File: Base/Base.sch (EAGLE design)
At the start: 20 parts

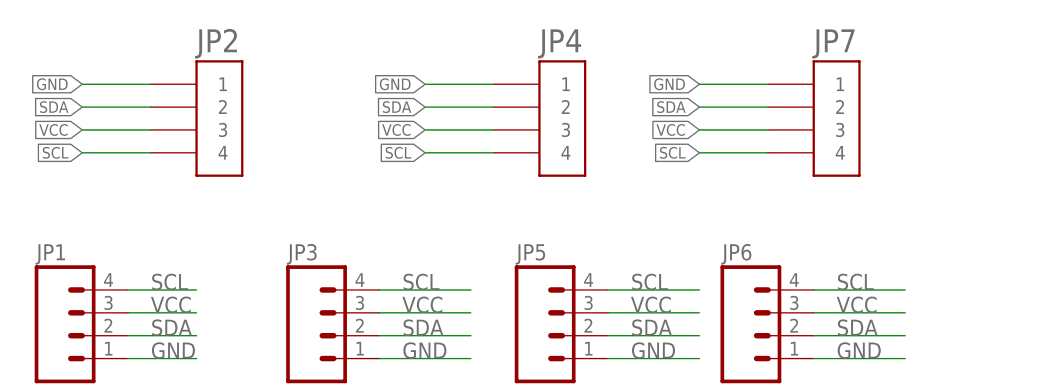
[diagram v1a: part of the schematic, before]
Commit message: Updated to grove compatible connector footprints
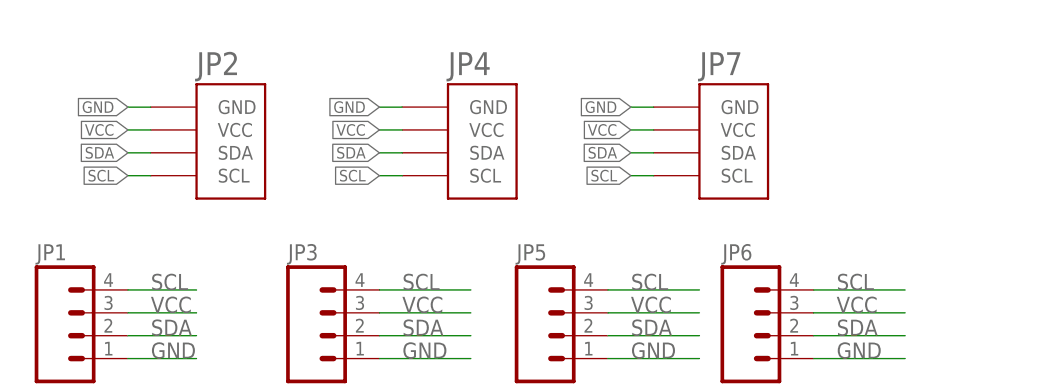
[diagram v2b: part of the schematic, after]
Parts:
- JP2, JP4, JP7: value HEADER-1X4-JST-PA-SIDE-SMD -> HEADER-MODULO; device Modulo:HEADER-1X4-JST-PA-SIDE-SMD -> Modulo:HEADER-MODULO
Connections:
- net GND: now also JP2.GND, JP4.GND, JP7.GND; no longer JP2.1, JP4.1, JP7.1
- net SCL: now also JP2.SCL, JP4.SCL, JP7.SCL; no longer JP2.4, JP4.4, JP7.4
- net SDA: now also JP2.SDA, JP4.SDA, JP7.SDA; no longer JP2.2, JP4.2, JP7.2
- net VCC: now also JP2.VCC, JP4.VCC, JP7.VCC; no longer JP2.3, JP4.3, JP7.3
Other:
- moved on the sheet: JP2, JP4, JP7
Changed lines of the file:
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@@
 <attribute name="NOBOM" value="1"/>
 </part>
-<part name="JP4" library="Modulo" deviceset="HEADER-1X4" device="-JST-PA-SIDE-SMD" value="HEADER-1X4-JST-PA-SIDE-SMD"/>
-<part name="JP7" library="Modulo" deviceset="HEADER-1X4" device="-JST-PA-SIDE-SMD" value="HEADER-1X4-JST-PA-SIDE-SMD"/>
-<part name="JP2" library="Modulo" deviceset="HEADER-1X4" device="-JST-PA-SIDE-SMD" value="HEADER-1X4-JST-PA-SIDE-SMD"/>
 <part name="H3" library="Modulo" deviceset="HOLE" device="#2" value="HOLE#2">
 <attribute name="NOBOM" value="1"/>
@@
 <part name="H8" library="Modulo" deviceset="HOLE" device="#2"/>
 <part name="H6" library="Modulo" deviceset="HOLE" device="#2"/>
+<part name="JP2" library="Modulo" deviceset="HEADER-MODULO" device=""/>
+<part name="JP4" library="Modulo" deviceset="HEADER-MODULO" device=""/>
+<part name="JP7" library="Modulo" deviceset="HEADER-MODULO" device=""/>
 </parts>
 <sheets>
@@
 <attribute name="NOBOM" x="152.4" y="81.28" size="1.016" layer="96" display="off"/>
 </instance>
-<instance part="JP4" gate="G$1" x="124.46" y="147.32"/>
-<instance part="JP7" gate="G$1" x="154.94" y="147.32"/>
-<instance part="JP2" gate="G$1" x="86.36" y="147.32"/>
 <instance part="H3" gate="G$1" x="162.56" y="81.28">
 <attribute name="NOBOM" x="162.56" y="81.28" size="1.016" layer="96" display="off"/>
@@
 <instance part="H8" gate="G$1" x="182.88" y="73.66"/>
 <instance part="H6" gate="G$1" x="172.72" y="73.66"/>
+<instance part="JP2" gate="G$1" x="88.9" y="142.24"/>
+<instance part="JP4" gate="G$1" x="116.84" y="142.24"/>
+<instance part="JP7" gate="G$1" x="144.78" y="142.24"/>
 </instances>
 <busses>
@@
 </segment>
 <segment>
-<wire x1="149.86" y1="144.78" x2="142.24" y2="144.78" width="0.1524" layer="91"/>
-<label x="142.24" y="144.78" size="1.27" layer="95" rot="R180" xref="yes"/>
-<pinref part="JP7" gate="G$1" pin="3"/>
-</segment>
-<segment>
-<wire x1="81.28" y1="144.78" x2="73.66" y2="144.78" width="0.1524" layer="91"/>
-<label x="73.66" y="144.78" size="1.27" layer="95" rot="R180" xref="yes"/>
-<pinref part="JP2" gate="G$1" pin="3"/>
-</segment>
-<segment>
-<wire x1="119.38" y1="144.78" x2="111.76" y2="144.78" width="0.1524" layer="91"/>
-<label x="111.76" y="144.78" size="1.27" layer="95" rot="R180" xref="yes"/>
-<pinref part="JP4" gate="G$1" pin="3"/>
+<pinref part="JP2" gate="G$1" pin="VCC"/>
+<wire x1="81.28" y1="144.78" x2="78.74" y2="144.78" width="0.1524" layer="91"/>
+<label x="78.74" y="144.78" size="1.27" layer="95" rot="R180" xref="yes"/>
+</segment>
+<segment>
+<pinref part="JP4" gate="G$1" pin="VCC"/>
+<wire x1="109.22" y1="144.78" x2="106.68" y2="144.78" width="0.1524" layer="91"/>
+<label x="106.68" y="144.78" size="1.27" layer="95" rot="R180" xref="yes"/>
+</segment>
+<segment>
+<pinref part="JP7" gate="G$1" pin="VCC"/>
+<wire x1="137.16" y1="144.78" x2="134.62" y2="144.78" width="0.1524" layer="91"/>
+<label x="134.62" y="144.78" size="1.27" layer="95" rot="R180" xref="yes"/>
 </segment>
 </net>
@@
 </segment>
 <segment>
-<wire x1="149.86" y1="149.86" x2="142.24" y2="149.86" width="0.1524" layer="91"/>
-<label x="142.24" y="149.86" size="1.27" layer="95" rot="R180" xref="yes"/>
-<pinref part="JP7" gate="G$1" pin="1"/>
-</segment>
-<segment>
-<wire x1="81.28" y1="149.86" x2="73.66" y2="149.86" width="0.1524" layer="91"/>
-<label x="73.66" y="149.86" size="1.27" layer="95" rot="R180" xref="yes"/>
-<pinref part="JP2" gate="G$1" pin="1"/>
-</segment>
-<segment>
-<wire x1="119.38" y1="149.86" x2="111.76" y2="149.86" width="0.1524" layer="91"/>
-<label x="111.76" y="149.86" size="1.27" layer="95" rot="R180" xref="yes"/>
-<pinref part="JP4" gate="G$1" pin="1"/>
+<pinref part="JP2" gate="G$1" pin="GND"/>
+<wire x1="81.28" y1="147.32" x2="78.74" y2="147.32" width="0.1524" layer="91"/>
+<label x="78.74" y="147.32" size="1.27" layer="95" rot="R180" xref="yes"/>
+</segment>
+<segment>
+<pinref part="JP4" gate="G$1" pin="GND"/>
+<wire x1="109.22" y1="147.32" x2="106.68" y2="147.32" width="0.1524" layer="91"/>
+<label x="106.68" y="147.32" size="1.27" layer="95" rot="R180" xref="yes"/>
+</segment>
+<segment>
+<pinref part="JP7" gate="G$1" pin="GND"/>
+<wire x1="137.16" y1="147.32" x2="134.62" y2="147.32" width="0.1524" layer="91"/>
+<label x="134.62" y="147.32" size="1.27" layer="95" rot="R180" xref="yes"/>
 </segment>
 </net>
@@
 </segment>
 <segment>
-<wire x1="149.86" y1="147.32" x2="142.24" y2="147.32" width="0.1524" layer="91"/>
-<label x="142.24" y="147.32" size="1.27" layer="95" rot="R180" xref="yes"/>
-<pinref part="JP7" gate="G$1" pin="2"/>
-</segment>
-<segment>
-<wire x1="81.28" y1="147.32" x2="73.66" y2="147.32" width="0.1524" layer="91"/>
-<label x="73.66" y="147.32" size="1.27" layer="95" rot="R180" xref="yes"/>
-<pinref part="JP2" gate="G$1" pin="2"/>
-</segment>
-<segment>
-<wire x1="119.38" y1="147.32" x2="111.76" y2="147.32" width="0.1524" layer="91"/>
-<label x="111.76" y="147.32" size="1.27" layer="95" rot="R180" xref="yes"/>
-<pinref part="JP4" gate="G$1" pin="2"/>
+<pinref part="JP2" gate="G$1" pin="SDA"/>
+<wire x1="81.28" y1="142.24" x2="78.74" y2="142.24" width="0.1524" layer="91"/>
+<label x="78.74" y="142.24" size="1.27" layer="95" rot="R180" xref="yes"/>
+</segment>
+<segment>
+<pinref part="JP4" gate="G$1" pin="SDA"/>
+<wire x1="109.22" y1="142.24" x2="106.68" y2="142.24" width="0.1524" layer="91"/>
+<label x="106.68" y="142.24" size="1.27" layer="95" rot="R180" xref="yes"/>
+</segment>
+<segment>
+<pinref part="JP7" gate="G$1" pin="SDA"/>
+<wire x1="137.16" y1="142.24" x2="134.62" y2="142.24" width="0.1524" layer="91"/>
+<label x="134.62" y="142.24" size="1.27" layer="95" rot="R180" xref="yes"/>
 </segment>
 </net>
@@
 </segment>
 <segment>
-<wire x1="149.86" y1="142.24" x2="142.24" y2="142.24" width="0.1524" layer="91"/>
-<label x="142.24" y="142.24" size="1.27" layer="95" rot="R180" xref="yes"/>
-<pinref part="JP7" gate="G$1" pin="4"/>
-</segment>
-<segment>
-<wire x1="81.28" y1="142.24" x2="73.66" y2="142.24" width="0.1524" layer="91"/>
-<label x="73.66" y="142.24" size="1.27" layer="95" rot="R180" xref="yes"/>
-<pinref part="JP2" gate="G$1" pin="4"/>
-</segment>
-<segment>
-<wire x1="119.38" y1="142.24" x2="111.76" y2="142.24" width="0.1524" layer="91"/>
-<label x="111.76" y="142.24" size="1.27" layer="95" rot="R180" xref="yes"/>
-<pinref part="JP4" gate="G$1" pin="4"/>
-</segment>
-</net>
+<pinref part="JP2" gate="G$1" pin="SCL"/>
+<wire x1="81.28" y1="139.7" x2="78.74" y2="139.7" width="0.1524" layer="91"/>
+<label x="78.74" y="139.7" size="1.27" layer="95" rot="R180" xref="yes"/>
+</segment>
+<segment>
+<pinref part="JP4" gate="G$1" pin="SCL"/>
+<wire x1="109.22" y1="139.7" x2="106.68" y2="139.7" width="0.1524" layer="91"/>
+<label x="106.68" y="139.7" size="1.27" layer="95" rot="R180" xref="yes"/>
+</segment>
+<segment>
+<pinref part="JP7" gate="G$1" pin="SCL"/>
+<wire x1="137.16" y1="139.7" x2="134.62" y2="139.7" width="0.1524" layer="91"/>
+<label x="134.62" y="139.7" size="1.27" layer="95" rot="R180" xref="yes"/>
+</segment>
+</net>

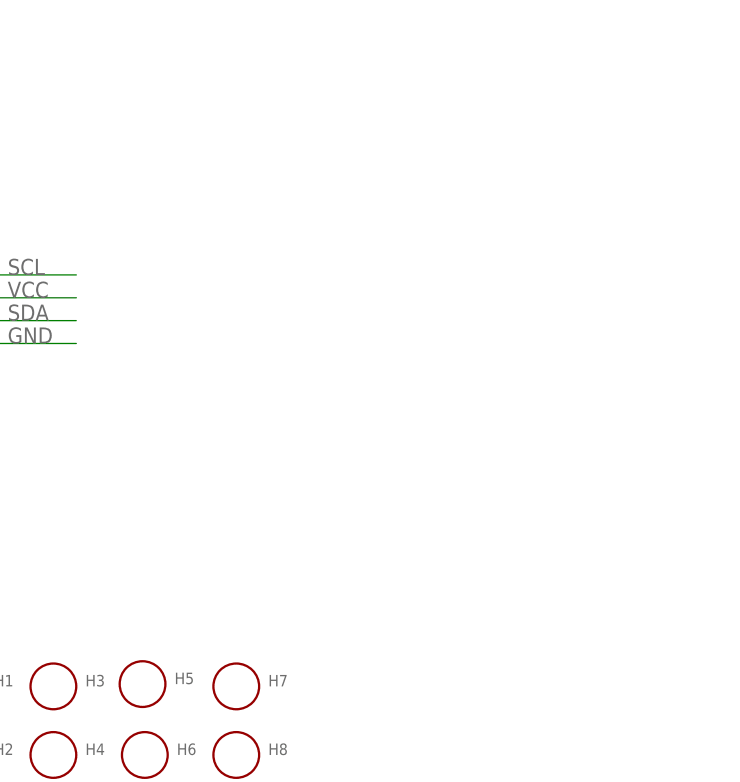
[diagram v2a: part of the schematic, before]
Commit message: Tented vias Updated extension cable connectors Added 3.3v regulator and clamping diodes
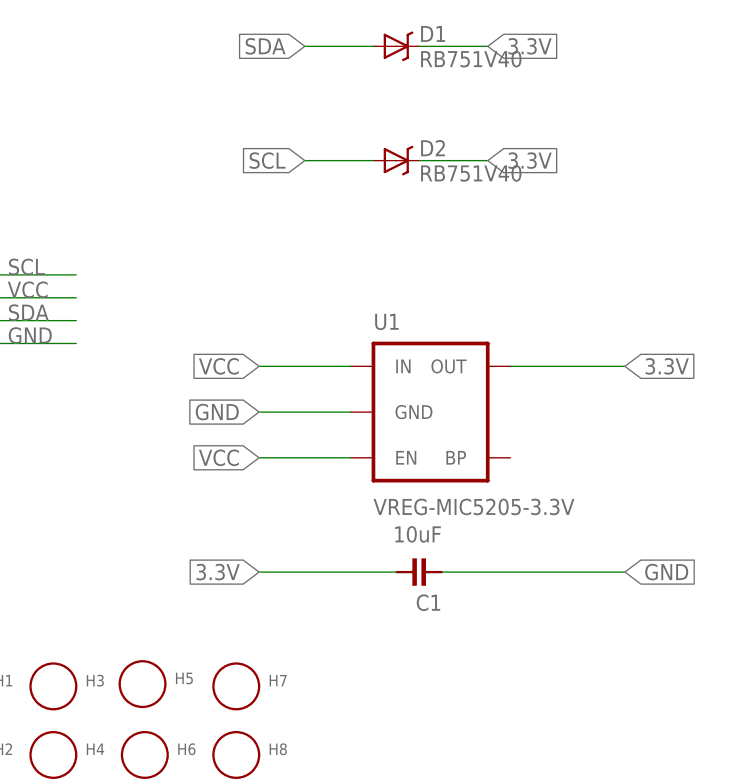
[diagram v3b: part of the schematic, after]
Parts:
- added C1: 10uF, Modulo:CAPACITOR-10UF
- added D1, D2: RB751V40, Modulo:DIODE-SCHOTTKY-BAT60A
- added U1: VREG-MIC5205-3.3V, Modulo:VREG-MIC5205-3.3V
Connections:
- new net 3.3V: C1.1, D1.C, D2.C, U1.OUT
- net GND: now also C1.2, U1.GND
- net SCL: now also D2.A
- net SDA: now also D1.A
- net VCC: now also U1.EN, U1.IN
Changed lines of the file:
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@@
 <part name="JP4" library="Modulo" deviceset="HEADER-MODULO" device=""/>
 <part name="JP7" library="Modulo" deviceset="HEADER-MODULO" device=""/>
+<part name="D1" library="Modulo" deviceset="DIODE-SCHOTTKY" device="-BAT60A" value="RB751V40">
+<attribute name="PARTNUM" value="RB751V40"/>
+</part>
+<part name="D2" library="Modulo" deviceset="DIODE-SCHOTTKY" device="-BAT60A" value="RB751V40">
+<attribute name="PARTNUM" value="RB751V40"/>
+</part>
+<part name="U1" library="Modulo" deviceset="VREG-MIC5205" device="-3.3V"/>
+<part name="C1" library="Modulo" deviceset="CAPACITOR" device="-10UF" value="10uF"/>
 </parts>
 <sheets>
@@
 <instance part="JP4" gate="G$1" x="116.84" y="142.24"/>
 <instance part="JP7" gate="G$1" x="144.78" y="142.24"/>
+<instance part="D1" gate="G$1" x="200.66" y="152.4"/>
+<instance part="D2" gate="G$1" x="200.66" y="139.7"/>
+<instance part="U1" gate="G$1" x="205.74" y="111.76"/>
+<instance part="C1" gate="G$1" x="203.2" y="93.98" rot="R90"/>
 </instances>
 <busses>
@@
 <label x="134.62" y="144.78" size="1.27" layer="95" rot="R180" xref="yes"/>
 </segment>
+<segment>
+<pinref part="U1" gate="G$1" pin="IN"/>
+<wire x1="195.58" y1="116.84" x2="185.42" y2="116.84" width="0.1524" layer="91"/>
+<label x="185.42" y="116.84" size="1.778" layer="95" rot="R180" xref="yes"/>
+</segment>
+<segment>
+<pinref part="U1" gate="G$1" pin="EN"/>
+<wire x1="195.58" y1="106.68" x2="185.42" y2="106.68" width="0.1524" layer="91"/>
+<label x="185.42" y="106.68" size="1.778" layer="95" rot="R180" xref="yes"/>
+</segment>
 </net>
 <net name="GND" class="0">
@@
 <label x="134.62" y="147.32" size="1.27" layer="95" rot="R180" xref="yes"/>
 </segment>
+<segment>
+<pinref part="U1" gate="G$1" pin="GND"/>
+<wire x1="195.58" y1="111.76" x2="185.42" y2="111.76" width="0.1524" layer="91"/>
+<label x="185.42" y="111.76" size="1.778" layer="95" rot="R180" xref="yes"/>
+</segment>
+<segment>
+<pinref part="C1" gate="G$1" pin="2"/>
+<wire x1="205.74" y1="93.98" x2="226.06" y2="93.98" width="0.1524" layer="91"/>
+<label x="226.06" y="93.98" size="1.778" layer="95" xref="yes"/>
+</segment>
 </net>
 <net name="SDA" class="0">
@@
 <label x="134.62" y="142.24" size="1.27" layer="95" rot="R180" xref="yes"/>
 </segment>
+<segment>
+<pinref part="D1" gate="G$1" pin="A"/>
+<wire x1="198.12" y1="152.4" x2="190.5" y2="152.4" width="0.1524" layer="91"/>
+<label x="190.5" y="152.4" size="1.778" layer="95" rot="R180" xref="yes"/>
+</segment>
 </net>
 <net name="SCL" class="0">
@@
 <label x="134.62" y="139.7" size="1.27" layer="95" rot="R180" xref="yes"/>
 </segment>
-</net>
+<segment>
+<pinref part="D2" gate="G$1" pin="A"/>
+<wire x1="198.12" y1="139.7" x2="190.5" y2="139.7" width="0.1524" layer="91"/>
+<label x="190.5" y="139.7" size="1.778" layer="95" rot="R180" xref="yes"/>
+</segment>
+</net>
+<net name="3.3V" class="0">
+<segment>
+<pinref part="C1" gate="G$1" pin="1"/>
+<wire x1="200.66" y1="93.98" x2="185.42" y2="93.98" width="0.1524" layer="91"/>
+<label x="185.42" y="93.98" size="1.778" layer="95" rot="R180" xref="yes"/>
+</segment>
+<segment>
+<pinref part="U1" gate="G$1" pin="OUT"/>
+<wire x1="213.36" y1="116.84" x2="226.06" y2="116.84" width="0.1524" layer="91"/>
+<label x="226.06" y="116.84" size="1.778" layer="95" xref="yes"/>
+</segment>
+<segment>
+<pinref part="D1" gate="G$1" pin="C"/>
+<wire x1="203.2" y1="152.4" x2="210.82" y2="152.4" width="0.1524" layer="91"/>
+<label x="210.82" y="152.4" size="1.778" layer="95" xref="yes"/>
+</segment>
+<segment>
+<pinref part="D2" gate="G$1" pin="C"/>
+<wire x1="203.2" y1="139.7" x2="210.82" y2="139.7" width="0.1524" layer="91"/>
+<label x="210.82" y="139.7" size="1.778" layer="95" xref="yes"/>
+</segment>
+</net>

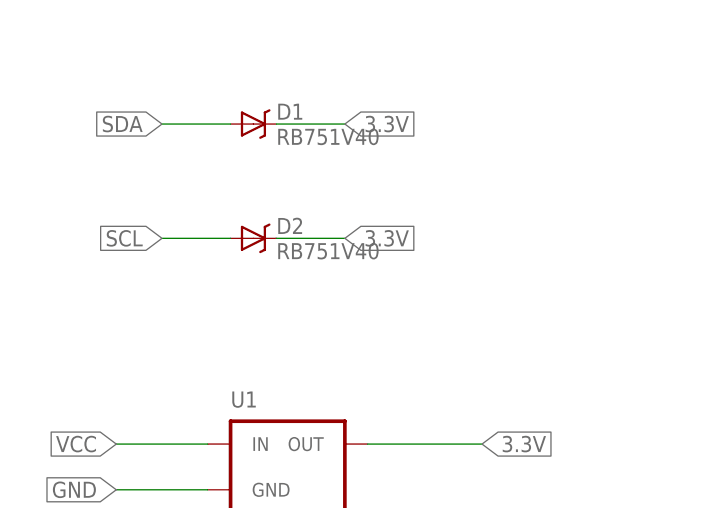
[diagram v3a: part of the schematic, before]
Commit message: Various small tweaks based on testing and feedback from manufacturer.
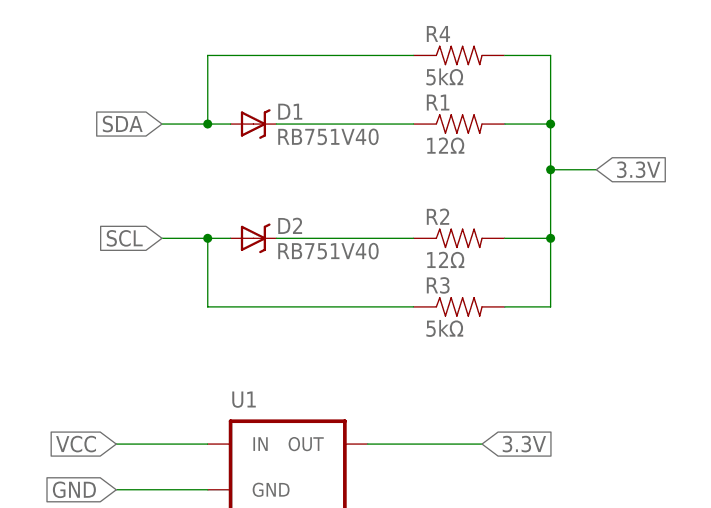
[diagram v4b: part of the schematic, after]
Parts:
- added R1, R2: 12Ω, Modulo:RESISTOR-12Ω
- added R3, R4: 5kΩ, Modulo:RESISTOR-5KΩ
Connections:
- new net N$1: D2.C, R2.1
- new net N$3: D1.C, R1.1
- net 3.3V: now also R1.2, R2.2, R3.2, R4.2; no longer D1.C, D2.C
- net SCL: now also R3.1
- net SDA: now also R4.1
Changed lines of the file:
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@@
 <part name="U1" library="Modulo" deviceset="VREG-MIC5205" device="-3.3V"/>
 <part name="C1" library="Modulo" deviceset="CAPACITOR" device="-10UF" value="10uF"/>
+<part name="R1" library="Modulo" deviceset="RESISTOR" device="-12Ω" value="12Ω"/>
+<part name="R2" library="Modulo" deviceset="RESISTOR" device="-12Ω" value="12Ω"/>
+<part name="R3" library="Modulo" deviceset="RESISTOR" device="-5KΩ" value="5kΩ"/>
+<part name="R4" library="Modulo" deviceset="RESISTOR" device="-5KΩ" value="5kΩ"/>
 </parts>
 <sheets>
@@
 <instance part="U1" gate="G$1" x="205.74" y="111.76"/>
 <instance part="C1" gate="G$1" x="203.2" y="93.98" rot="R90"/>
+<instance part="R1" gate="G$1" x="223.52" y="152.4"/>
+<instance part="R2" gate="G$1" x="223.52" y="139.7"/>
+<instance part="R3" gate="G$1" x="223.52" y="132.08"/>
+<instance part="R4" gate="G$1" x="223.52" y="160.02"/>
 </instances>
 <busses>
@@
 <segment>
 <pinref part="D1" gate="G$1" pin="A"/>
-<wire x1="198.12" y1="152.4" x2="190.5" y2="152.4" width="0.1524" layer="91"/>
+<wire x1="198.12" y1="152.4" x2="195.58" y2="152.4" width="0.1524" layer="91"/>
 <label x="190.5" y="152.4" size="1.778" layer="95" rot="R180" xref="yes"/>
+<pinref part="R4" gate="G$1" pin="1"/>
+<wire x1="195.58" y1="152.4" x2="190.5" y2="152.4" width="0.1524" layer="91"/>
+<wire x1="218.44" y1="160.02" x2="195.58" y2="160.02" width="0.1524" layer="91"/>
+<wire x1="195.58" y1="160.02" x2="195.58" y2="152.4" width="0.1524" layer="91"/>
+<junction x="195.58" y="152.4"/>
 </segment>
 </net>
@@
 <segment>
 <pinref part="D2" gate="G$1" pin="A"/>
-<wire x1="198.12" y1="139.7" x2="190.5" y2="139.7" width="0.1524" layer="91"/>
+<wire x1="198.12" y1="139.7" x2="195.58" y2="139.7" width="0.1524" layer="91"/>
 <label x="190.5" y="139.7" size="1.778" layer="95" rot="R180" xref="yes"/>
+<pinref part="R3" gate="G$1" pin="1"/>
+<wire x1="195.58" y1="139.7" x2="190.5" y2="139.7" width="0.1524" layer="91"/>
+<wire x1="218.44" y1="132.08" x2="195.58" y2="132.08" width="0.1524" layer="91"/>
+<wire x1="195.58" y1="132.08" x2="195.58" y2="139.7" width="0.1524" layer="91"/>
+<junction x="195.58" y="139.7"/>
 </segment>
 </net>
@@
 </segment>
 <segment>
+<pinref part="R3" gate="G$1" pin="2"/>
+<wire x1="228.6" y1="132.08" x2="233.68" y2="132.08" width="0.1524" layer="91"/>
+<wire x1="233.68" y1="132.08" x2="233.68" y2="139.7" width="0.1524" layer="91"/>
+<pinref part="R4" gate="G$1" pin="2"/>
+<wire x1="233.68" y1="139.7" x2="233.68" y2="147.32" width="0.1524" layer="91"/>
+<wire x1="233.68" y1="147.32" x2="233.68" y2="152.4" width="0.1524" layer="91"/>
+<wire x1="233.68" y1="152.4" x2="233.68" y2="160.02" width="0.1524" layer="91"/>
+<wire x1="233.68" y1="160.02" x2="228.6" y2="160.02" width="0.1524" layer="91"/>
+<pinref part="R1" gate="G$1" pin="2"/>
+<wire x1="228.6" y1="152.4" x2="233.68" y2="152.4" width="0.1524" layer="91"/>
+<pinref part="R2" gate="G$1" pin="2"/>
+<wire x1="228.6" y1="139.7" x2="233.68" y2="139.7" width="0.1524" layer="91"/>
+<wire x1="233.68" y1="147.32" x2="238.76" y2="147.32" width="0.1524" layer="91"/>
+<label x="238.76" y="147.32" size="1.778" layer="95" xref="yes"/>
+<junction x="233.68" y="152.4"/>
+<junction x="233.68" y="147.32"/>
+<junction x="233.68" y="139.7"/>
+</segment>
+</net>
+<net name="N$1" class="0">
+<segment>
+<pinref part="D2" gate="G$1" pin="C"/>
+<pinref part="R2" gate="G$1" pin="1"/>
+<wire x1="203.2" y1="139.7" x2="218.44" y2="139.7" width="0.1524" layer="91"/>
+</segment>
+</net>
+<net name="N$3" class="0">
+<segment>
+<pinref part="R1" gate="G$1" pin="1"/>
 <pinref part="D1" gate="G$1" pin="C"/>
-<wire x1="203.2" y1="152.4" x2="210.82" y2="152.4" width="0.1524" layer="91"/>
-<label x="210.82" y="152.4" size="1.778" layer="95" xref="yes"/>
-</segment>
-<segment>
-<pinref part="D2" gate="G$1" pin="C"/>
-<wire x1="203.2" y1="139.7" x2="210.82" y2="139.7" width="0.1524" layer="91"/>
-<label x="210.82" y="139.7" size="1.778" layer="95" xref="yes"/>
-</segment>
-</net>
+<wire x1="218.44" y1="152.4" x2="203.2" y2="152.4" width="0.1524" layer="91"/>
+</segment>
+</net>

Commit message: Added unique board prefixes to part numbers due to CM requirements
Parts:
- added 2-FOOT1, 2-FOOT2, 2-FOOT3, 2-FOOT4: FOOT, Modulo:FOOT
- renumbered C1 to 2-C1, D1 to 2-D1, D2 to 2-D2, F1 to 2-F1, F2 to 2-F2, G1 to 2-G1, G2 to 2-G2, G3 to 2-G3, JP1 to 2-JP1, JP2 to 2-JP2, JP3 to 2-JP3, JP4 to 2-JP4, JP5 to 2-JP5, JP6 to 2-JP6, JP7 to 2-JP7, R1 to 2-R1, R2 to 2-R2, R3 to 2-R3, R4 to 2-R4, U1 to 2-U1
